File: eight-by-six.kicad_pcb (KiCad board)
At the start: 2 copper layers, 171.4 x 171.4 mm, 98 parts, among them J1 Left, J2 Right, SW1 Key, SW10 Key, SW11 Key, SW12 Key, SW13 Key, SW14 Key, SW15 Key, SW16 Key, SW17 Key, SW18 Key, SW19 Key, SW2 Key, SW20 Key, SW21 Key, SW22 Key, SW23 Key, SW24 Key, SW25 Key, SW26 Key, SW27 Key, SW28 Key, SW29 Key, SW3 Key, SW30 Key, SW31 Key, SW32 Key, SW33 Key, SW34 Key, SW35 Key, SW36 Key, SW37 Key, SW38 Key, SW39 Key, SW4 Key, SW40 Key, SW41 Key, SW42 Key, SW43 Key, SW44 Key, SW45 Key, SW46 Key, SW47 Key, SW48 Key, SW5 Key, SW6 Key, SW7 Key, SW8 Key, SW9 Key

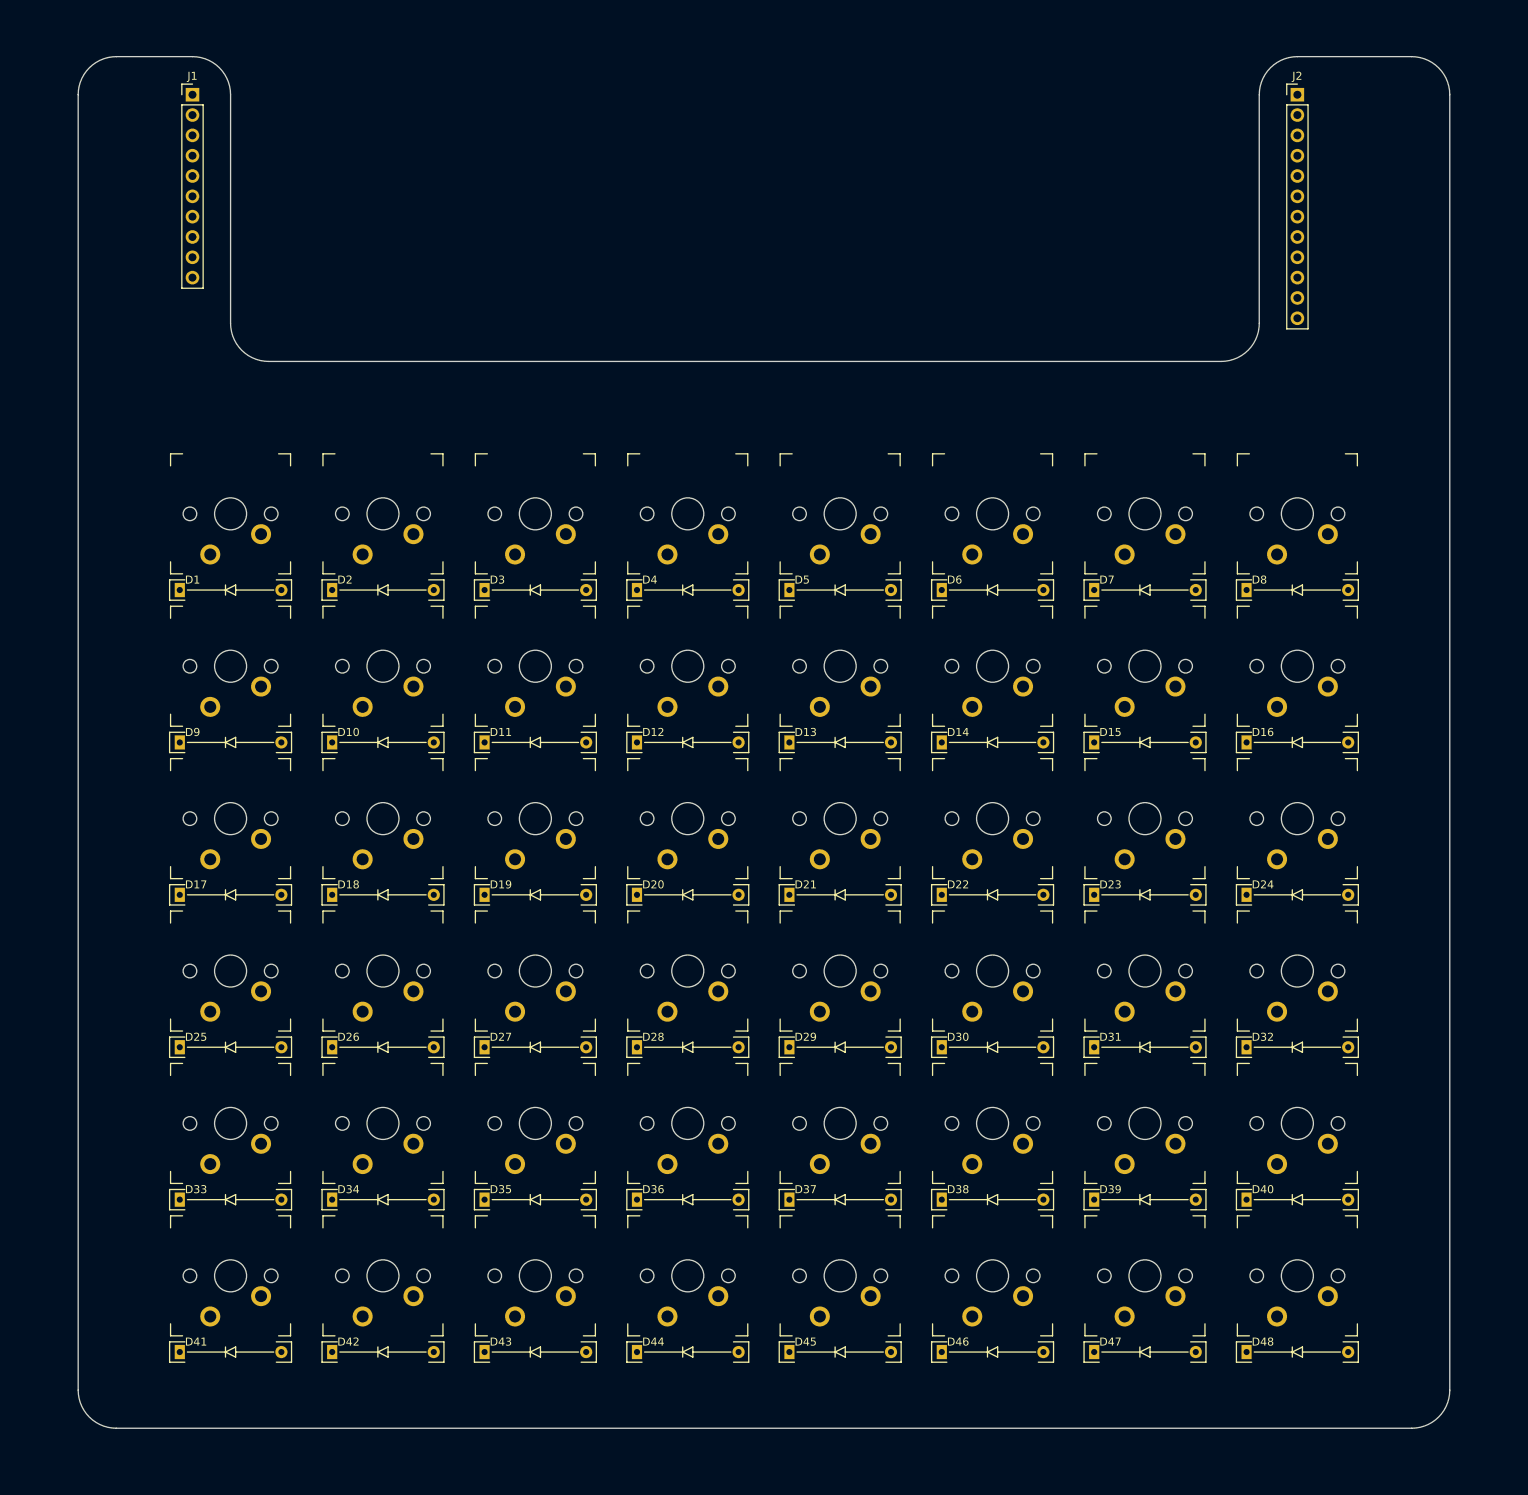
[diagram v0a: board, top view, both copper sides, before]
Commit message: add mounting holes, fixe shape, connector position, proto-traces from the connector
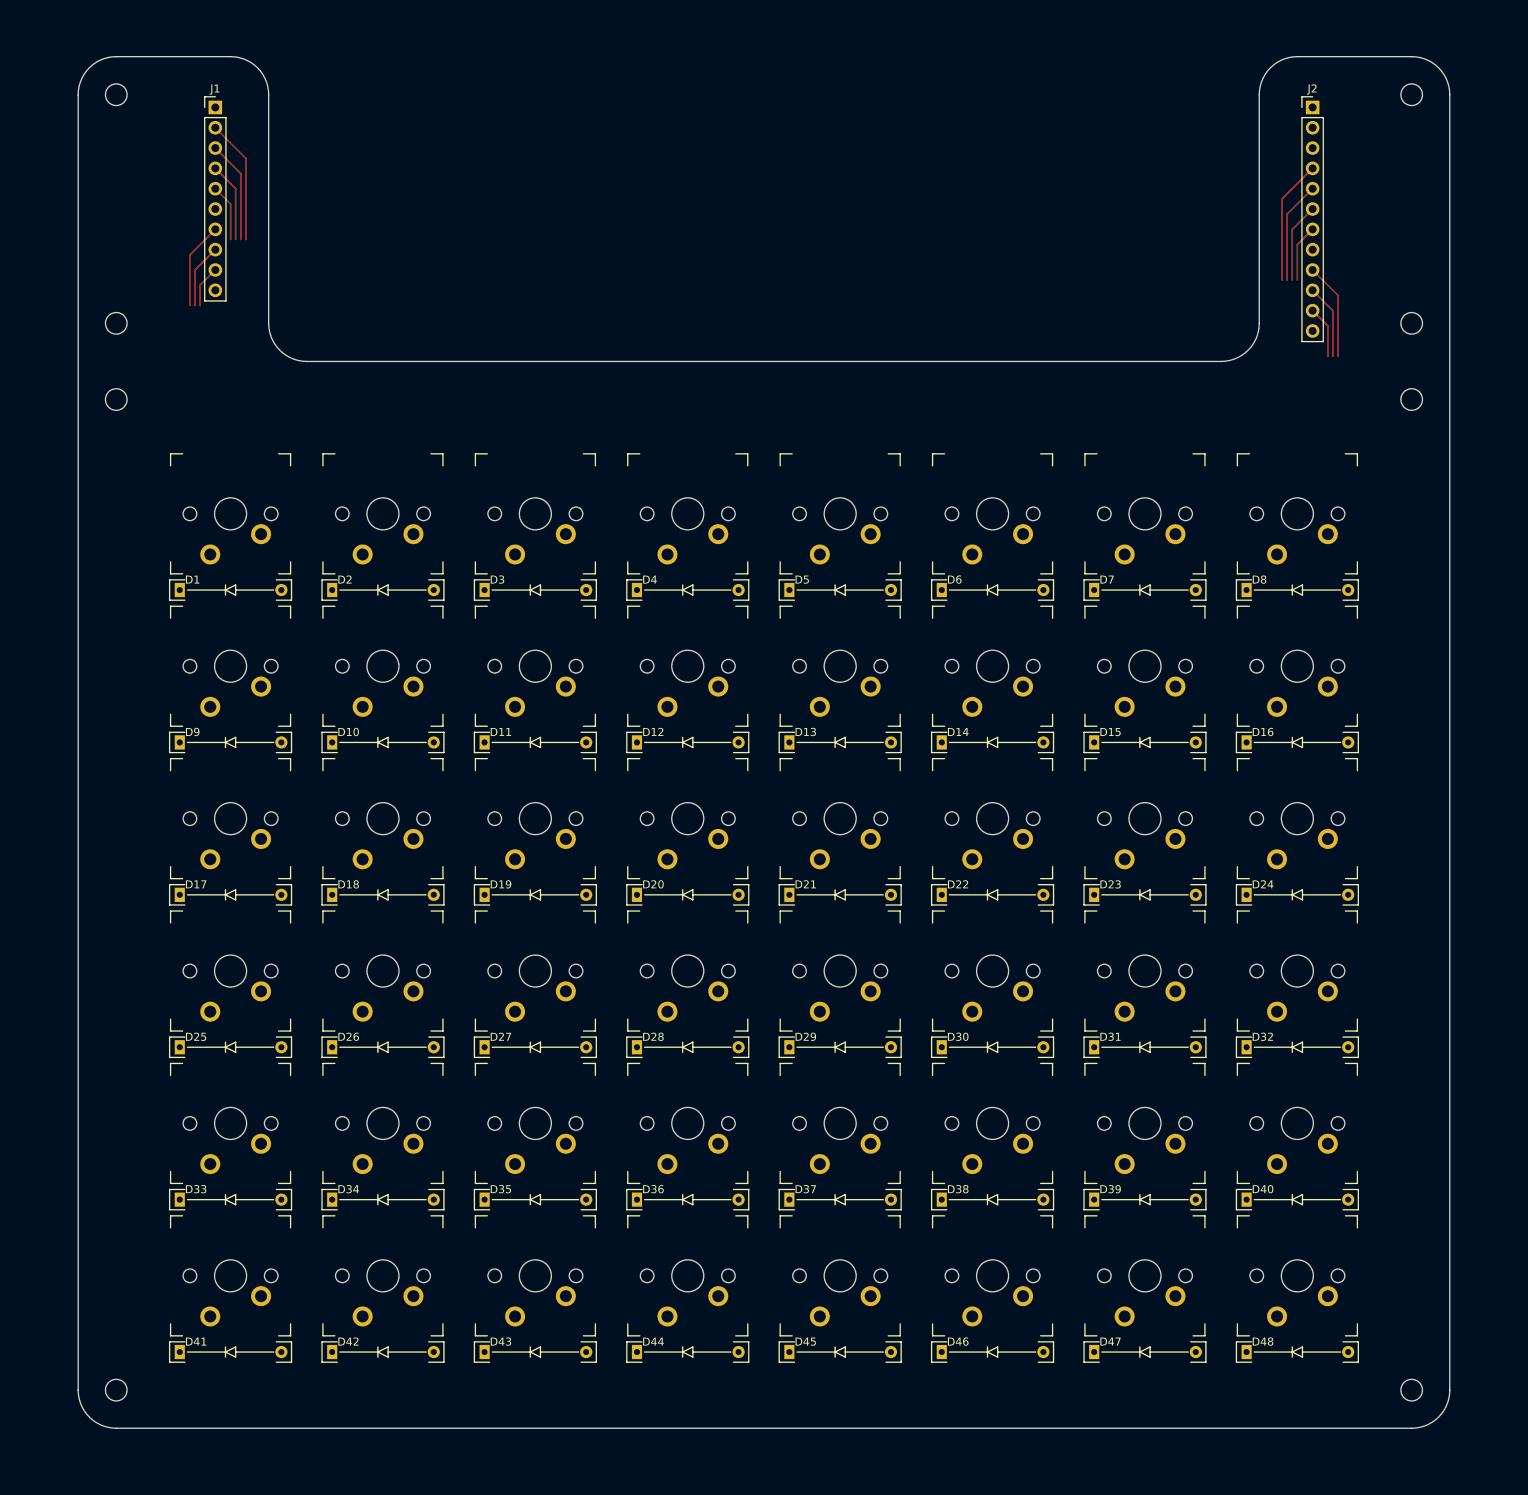
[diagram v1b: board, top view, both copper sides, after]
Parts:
- added H1: M2.5, MountingHole:MountingHole_2.7mm_M2.5, F.Cu at (23.8, 81.0)
- added H2: M2.5, MountingHole:MountingHole_2.7mm_M2.5, F.Cu at (23.8, 109.5)
- added H3: M2.5, MountingHole:MountingHole_2.7mm_M2.5, F.Cu at (23.8, 119.1)
- added H4: M2.5, MountingHole:MountingHole_2.7mm_M2.5, F.Cu at (23.8, 242.9)
- added H5: M2.5, MountingHole:MountingHole_2.7mm_M2.5, F.Cu at (185.7, 81.0)
- added H6: M2.5, MountingHole:MountingHole_2.7mm_M2.5, F.Cu at (185.7, 109.5)
- added H7: M2.5, MountingHole:MountingHole_2.7mm_M2.5, F.Cu at (185.7, 119.1)
- added H8: M2.5, MountingHole:MountingHole_2.7mm_M2.5, F.Cu at (185.7, 242.9)
- moved J1 3.27 mm to (36.2, 82.5)
- moved J2 2.48 mm to (173.4, 82.5)
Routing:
- net /c4: track 0.00 -> 15.5 mm
- net /c3: track 0.00 -> 15.5 mm
- net /c2: track 0.00 -> 12.7 mm
- net /c5: track 0.00 -> 12.7 mm
- net /r5: track 0.00 -> 12.1 mm
- net /r2: track 0.00 -> 10.8 mm
- net /c1: track 0.00 -> 9.94 mm
- net /c6: track 0.00 -> 9.94 mm
- net /r4: track 0.00 -> 9.31 mm
- net /r1: track 0.00 -> 8.04 mm
- net /c0: track 0.00 -> 7.14 mm
- net /c7: track 0.00 -> 7.14 mm
- net /r3: track 0.00 -> 6.50 mm
- net /r0: track 0.00 -> 5.23 mm
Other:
- outline, holes or cut-outs redrawn

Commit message: routing
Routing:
- net /r5: track 12.1 -> 284.1 mm
- net /r4: track 9.31 -> 262.0 mm
- net /r2: track 10.8 -> 246.9 mm, vias 0 -> 1
- net /r3: track 6.50 -> 240.3 mm
- net /r1: track 8.04 -> 225.2 mm, vias 0 -> 1
- net /r0: track 5.23 -> 203.1 mm, vias 0 -> 1
- net /c3: track 15.5 -> 205.2 mm, vias 0 -> 2
- net /c4: track 15.5 -> 193.4 mm, vias 0 -> 2
- net /c2: track 12.7 -> 184.5 mm, vias 0 -> 2
- net /c5: track 12.7 -> 172.6 mm, vias 0 -> 2
- net /c1: track 9.94 -> 163.7 mm, vias 0 -> 2
- net /c6: track 9.94 -> 151.4 mm, vias 0 -> 2
- net /c0: track 7.14 -> 142.9 mm
- net /c7: track 7.14 -> 139.2 mm
- added copper zone on B.Cu, net GND
- added copper zone on F.Cu, net GND

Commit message: done rooting ; TODO project labels : title, version, issue date, cc-0
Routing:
- net Net-(D9-K): track 0.00 -> 5.85 mm
- net Net-(D16-K): track 0.00 -> 5.85 mm
- net Net-(D15-K): track 0.00 -> 5.85 mm
- net Net-(D14-K): track 0.00 -> 5.85 mm
- net Net-(D13-K): track 0.00 -> 5.85 mm
- net Net-(D11-K): track 0.00 -> 5.85 mm
- net Net-(D10-K): track 0.00 -> 5.85 mm
- net Net-(D12-K): track 0.00 -> 5.85 mm
- net Net-(D8-K): track 0.00 -> 5.85 mm
- net Net-(D7-K): track 0.00 -> 5.85 mm
- net Net-(D6-K): track 0.00 -> 5.85 mm
- net Net-(D5-K): track 0.00 -> 5.85 mm
- net Net-(D48-K): track 0.00 -> 5.85 mm
- net Net-(D47-K): track 0.00 -> 5.85 mm
- net Net-(D46-K): track 0.00 -> 5.85 mm
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
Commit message: added measurement -- ready to release
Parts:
- added G***: LOGO, cliparts:logo--cc--cc, F.Cu at (102.2, 243.8)
- added G***: LOGO, cliparts:logo--cc--zero, F.Cu at (107.3, 243.8)
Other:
- board text added: "${COMMENT3}"
- board text added: "${TITLE}"
- board text added: "Version ${REVISION} -- ${ISSUE_DATE}"
- board text added: "WITHOUT ANY WARRANTY; without even the implied warranty of SAFETY, MERCHANTABILITY or FITNESS FOR A PARTICULAR PURPOSE."
